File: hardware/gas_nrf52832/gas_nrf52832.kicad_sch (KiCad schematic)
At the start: 0 parts

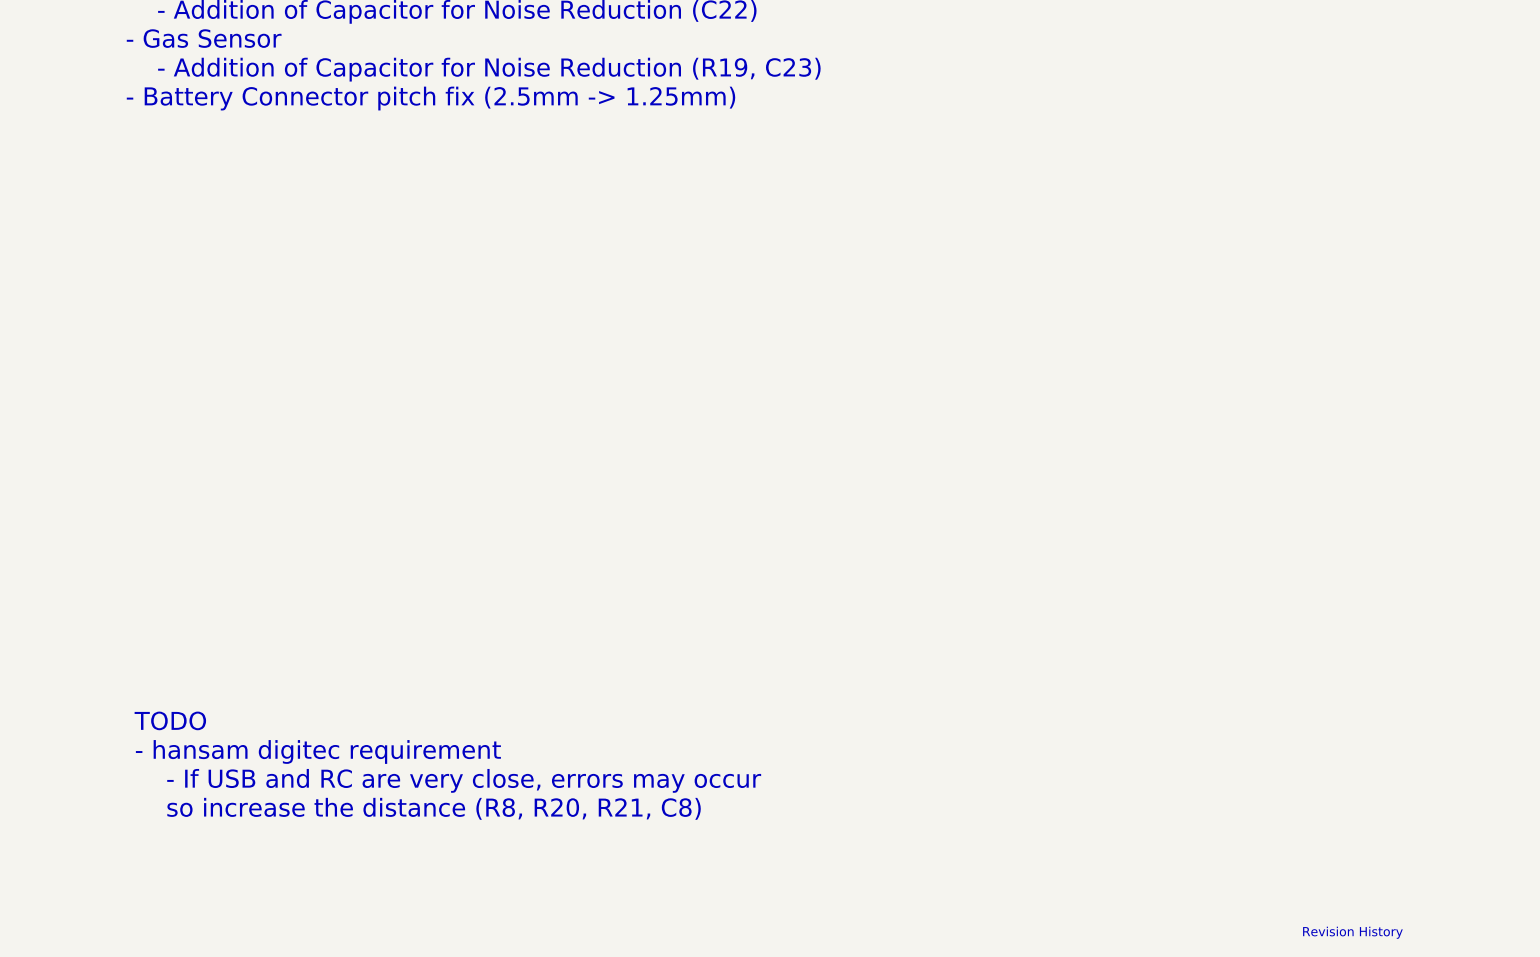
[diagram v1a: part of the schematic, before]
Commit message: feat: hw revision 1.0.2
Rev 1.0.2
- Oxygen Sensor
	- Voltage Amplification Ratio AdjustmentR18(10.7 -> 10k), R12(2.0k -> 2M)
	-> Reduce Current Consumption
	- Addition of lowpass filter for Noise Reduction
- Gas Sensor
	- Addition of lowpass filter for Noise Reduction
- 2 Layter -> 4 Layer
- hansam digitec requirement
	- If USB and RC are very close, errors may occur
	so increase the distance (R1, R23, R24, C22)
- BME680 Sensor Enable ctrl remove
- 32k Crystal Layout fix
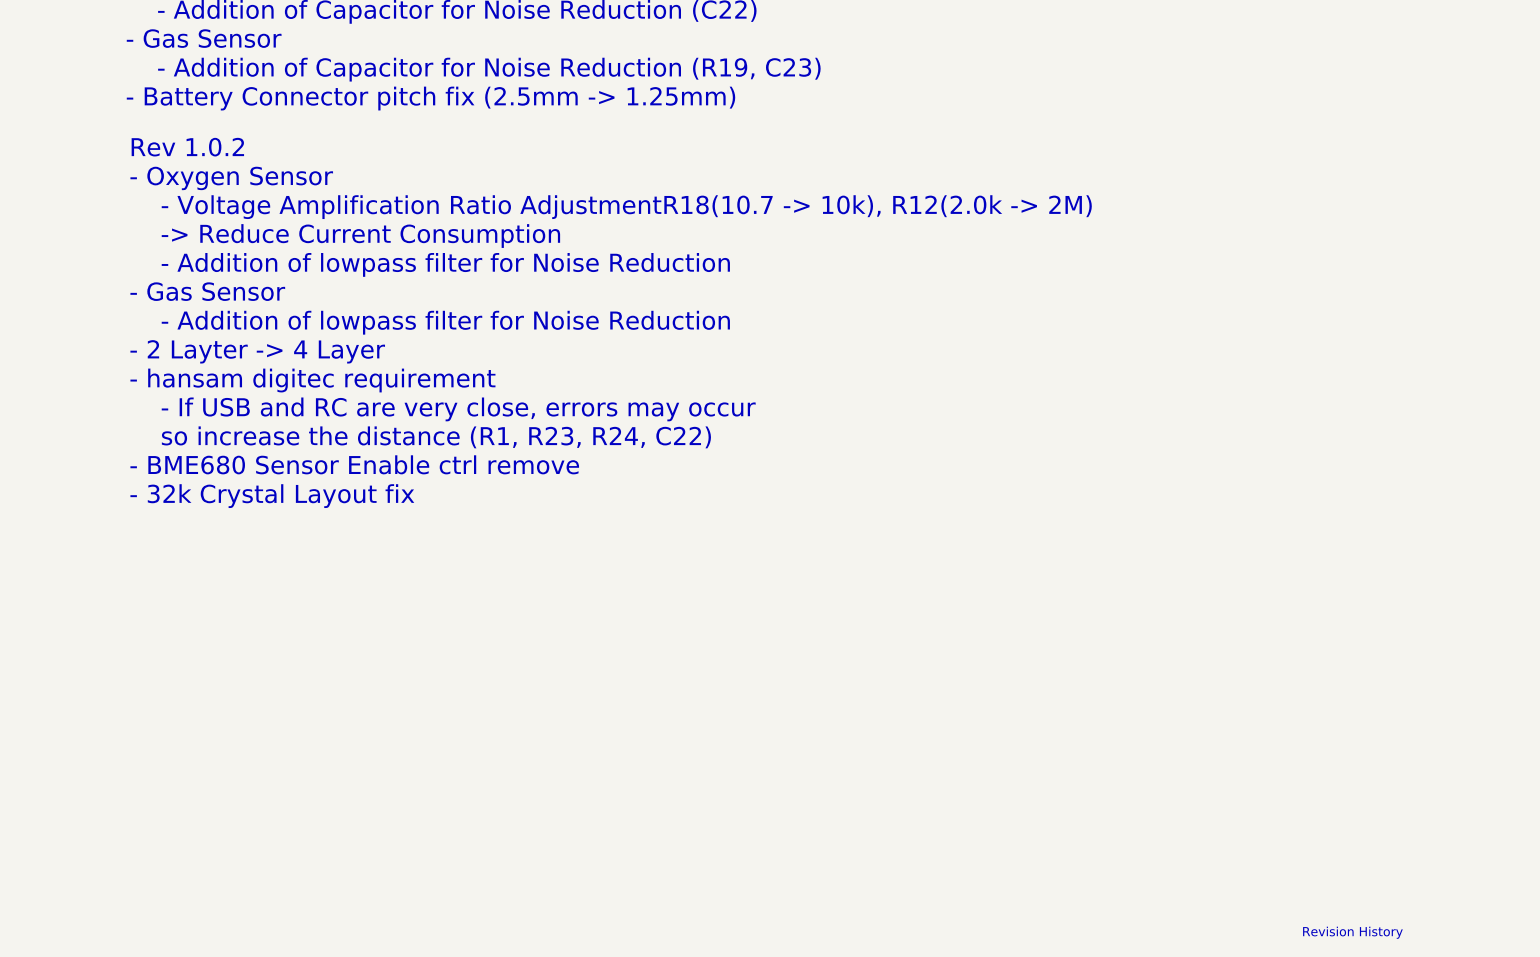
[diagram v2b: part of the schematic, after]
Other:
- note added: "Rev 1.0.2 - Oxygen Sensor - Voltage Amplification Ratio AdjustmentR18(10.7 -> 10k), R12(2.0k -> 2M) -> Reduce Current Consumption - Addition of lowpass filter for Noise Reduction - Gas Sensor - Addition of lowpass filter for Noise Reduction - 2 Layter -> 4 Layer - hansam digitec requirement - If USB and RC are very close, errors may occur so increase the distance (R1, R23, R24, C22) - BME680 Sens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"
- note removed: "TODO - hansam digitec requirement - If USB and RC are very close, errors may occur so increase the distance (R8, R20, R21, C8)"
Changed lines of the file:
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@@
 		)
 	)
-	(text "TODO\n- hansam digitec requirement\n	- If USB and RC are very close, errors may occur\n	so increase the distance (R8, R20, R21, C8)"
+	(text "Rev 1.0.2\n- Oxygen Sensor\n	- Voltage Amplification Ratio AdjustmentR18(10.7 -> 10k), R12(2.0k -> 2M)\n	-> Reduce Current Consumption\n	- Addition of lowpass filter for Noise Reduction\n- Gas Sensor\n	- Addition of lowpass filter for Noise Reduction\n- 2 Layter -> 4 Layer\n- hansam digitec requirement\n	- If USB and RC are very close, errors may occur\n	so increase the distance (R1, R23, R24, C22)\n- BME680 Sensor Enable ctrl remove\n- 32k Crystal Layout fix"
 		(exclude_from_sim no)
-		(at 24.13 173.99 0)
+		(at 23.368 130.302 0)
 		(effects
 			(font

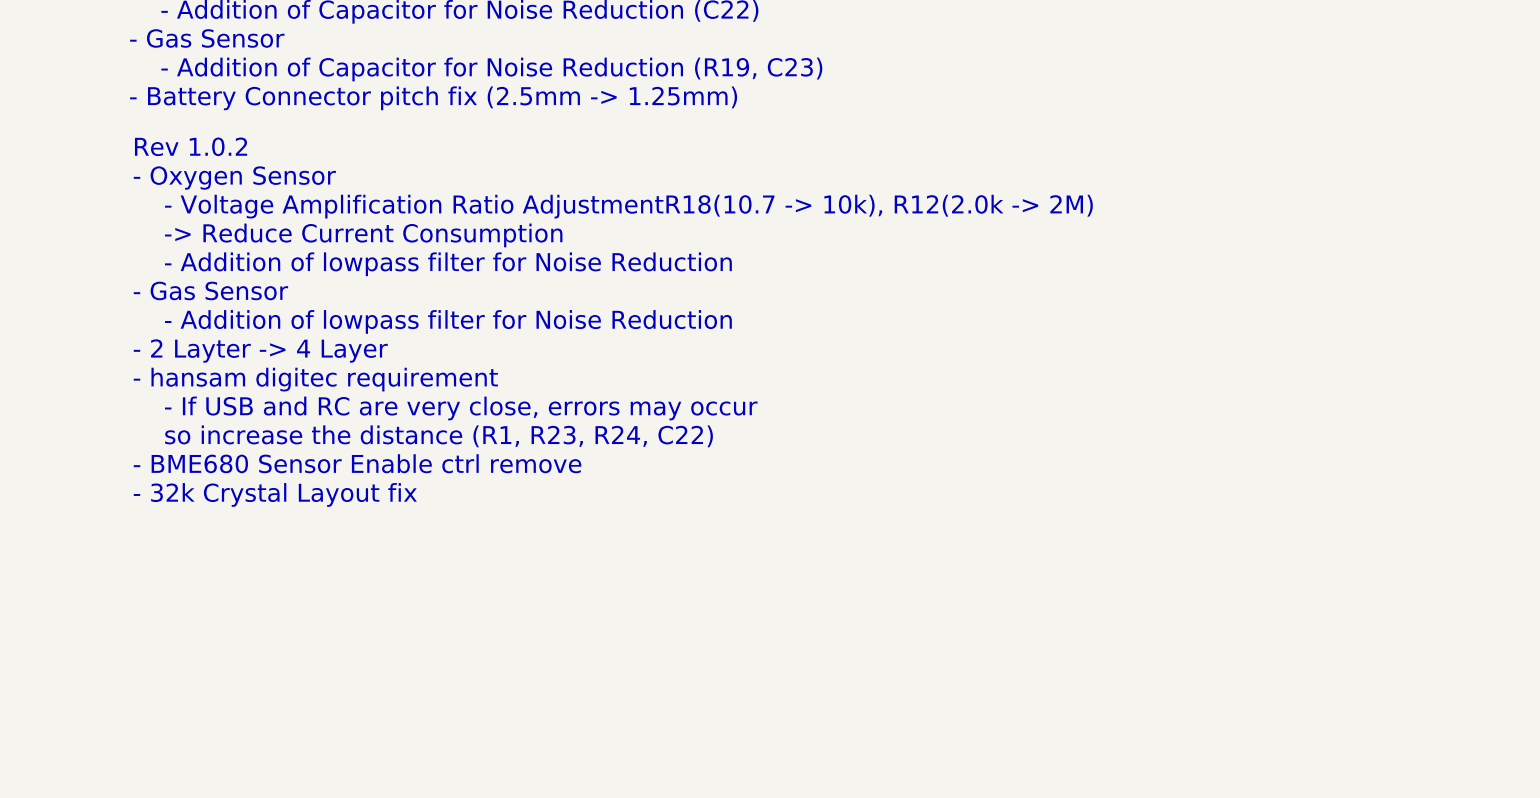
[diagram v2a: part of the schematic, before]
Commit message: feat: hw revision 1.0.3
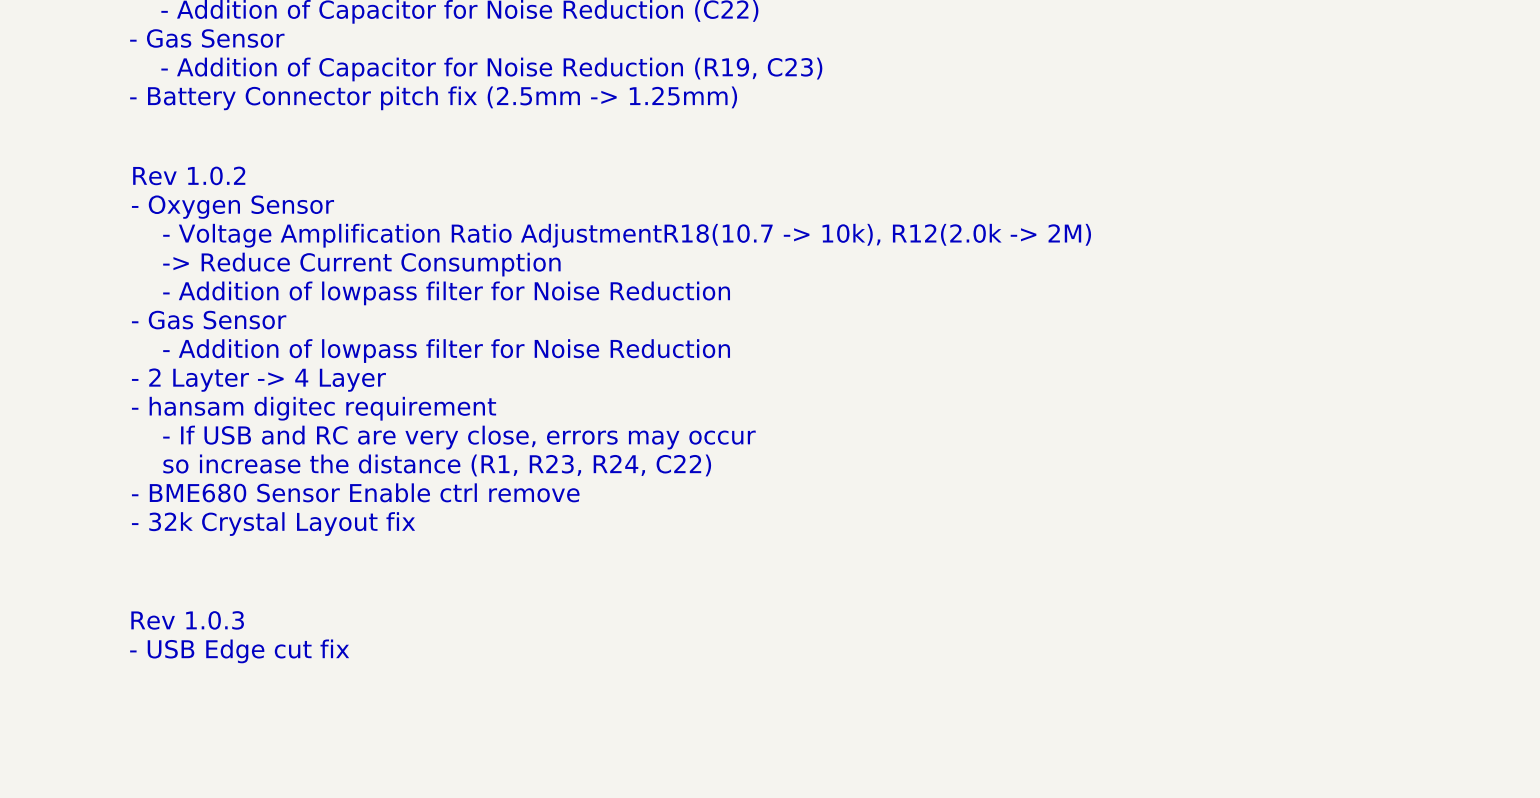
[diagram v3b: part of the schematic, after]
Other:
- note added: "Rev 1.0.3 - USB Edge cut fix"
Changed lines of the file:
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@@
 	(text "Rev 1.0.2\n- Oxygen Sensor\n	- Voltage Amplification Ratio AdjustmentR18(10.7 -> 10k), R12(2.0k -> 2M)\n	-> Reduce Current Consumption\n	- Addition of lowpass filter for Noise Reduction\n- Gas Sensor\n	- Addition of lowpass filter for Noise Reduction\n- 2 Layter -> 4 Layer\n- hansam digitec requirement\n	- If USB and RC are very close, errors may occur\n	so increase the distance (R1, R23, R24, C22)\n- BME680 Sensor Enable ctrl remove\n- 32k Crystal Layout fix"
 		(exclude_from_sim no)
-		(at 23.368 130.302 0)
+		(at 23.114 134.366 0)
 		(effects
 			(font
+				(size 2.5 2.5)
+			)
+			(justify left bottom)
+		)
+	)
+	(text "Rev 1.0.3\n- USB Edge cut fix"
+		(exclude_from_sim no)
+		(at 22.86 152.146 0)
+		(effects
+			(font
